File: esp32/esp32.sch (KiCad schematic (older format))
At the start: 54 parts, among them IC1 KF33BDT-TR, J1 USB_C_Receptacle_2.0, Q1 FDS9926A, Q2 FDN306P, Q3 BC817, Q4 BC817, SW1 ON-OFF, SW2 Reset, SW3 Boot, U1 AP5056, U2 DW01A, U3 CP2102, U4 ESP32-WROOM-32

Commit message: Add PCB routing
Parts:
- added J2, J3: Conn_01x16, Connector_PinHeader_2.54mm:PinHeader_1x16_P2.54mm_Vertical, symbol Connector_Generic:Conn_01x16
- BT1: footprint BatteryHolder:BatteryHolder_SMT_1x26650 -> TerminalBlock_MetzConnect:TerminalBlock_MetzConnect_Type055_RT01502HDWU_1x02_P5.00mm_Horizontal
- J1: value USB_C_Receptacle_2.0 -> USB_C
- SW3: footprint Button_Switch_SMD:SW_SPST_B3U-1000P-B -> Button_Switch_SMD:SW_SPST_B3U-1000P
- U1: symbol CP2102:AP5056 -> esp32-rescue:AP5056-CP2102
- U2: renamed from U3; symbol CP2102:CP2102 -> esp32-rescue:CP2102-CP2102
- renumbered C9 to C10, C10 to C11, C11 to C12, C3 to C13, C13 to C14, C4 to C3, C5 to C4, C12 to C5, C14 to C7, C7 to C8, C8 to C9, U4 to ESP32, Q2 to Q1, Q1 to Q2, R12 to R10, R13 to R11, R14 to R12, R15 to R13, R4 to R14, R16 to R15, R17 to R16, R18 to R17, R9 to R18, R5 to R4, R6 to R5, R7 to R6, R8 to R7, R10 to R8, R11 to R9, U2 to U3
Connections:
- net labels added: 10, 11, 12, 13, 14, 16, 23, 24, 26, 27, 28, 29, 30, 31, 33, 36, 37, 4, 5, 6, 7, 8, 9, Rx, Temp, Tx
- wire segments 228 -> 290
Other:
- note added: "3.3V Regulator"
- note added: "Auto-Reset"
- note added: "Battery Charger"
- note added: "Battery Protection"
- note added: "Pin connector"
- note added: "Reset & Boot"
- note added: "USB to UART Bridge"
- note added: "USB-C Connector"
- note added: "Wi-Fi+BT Module"
- moved on the sheet: BT1, C1, C10, C11, C12, C13, C14, C2, C3, C4, C5, C6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

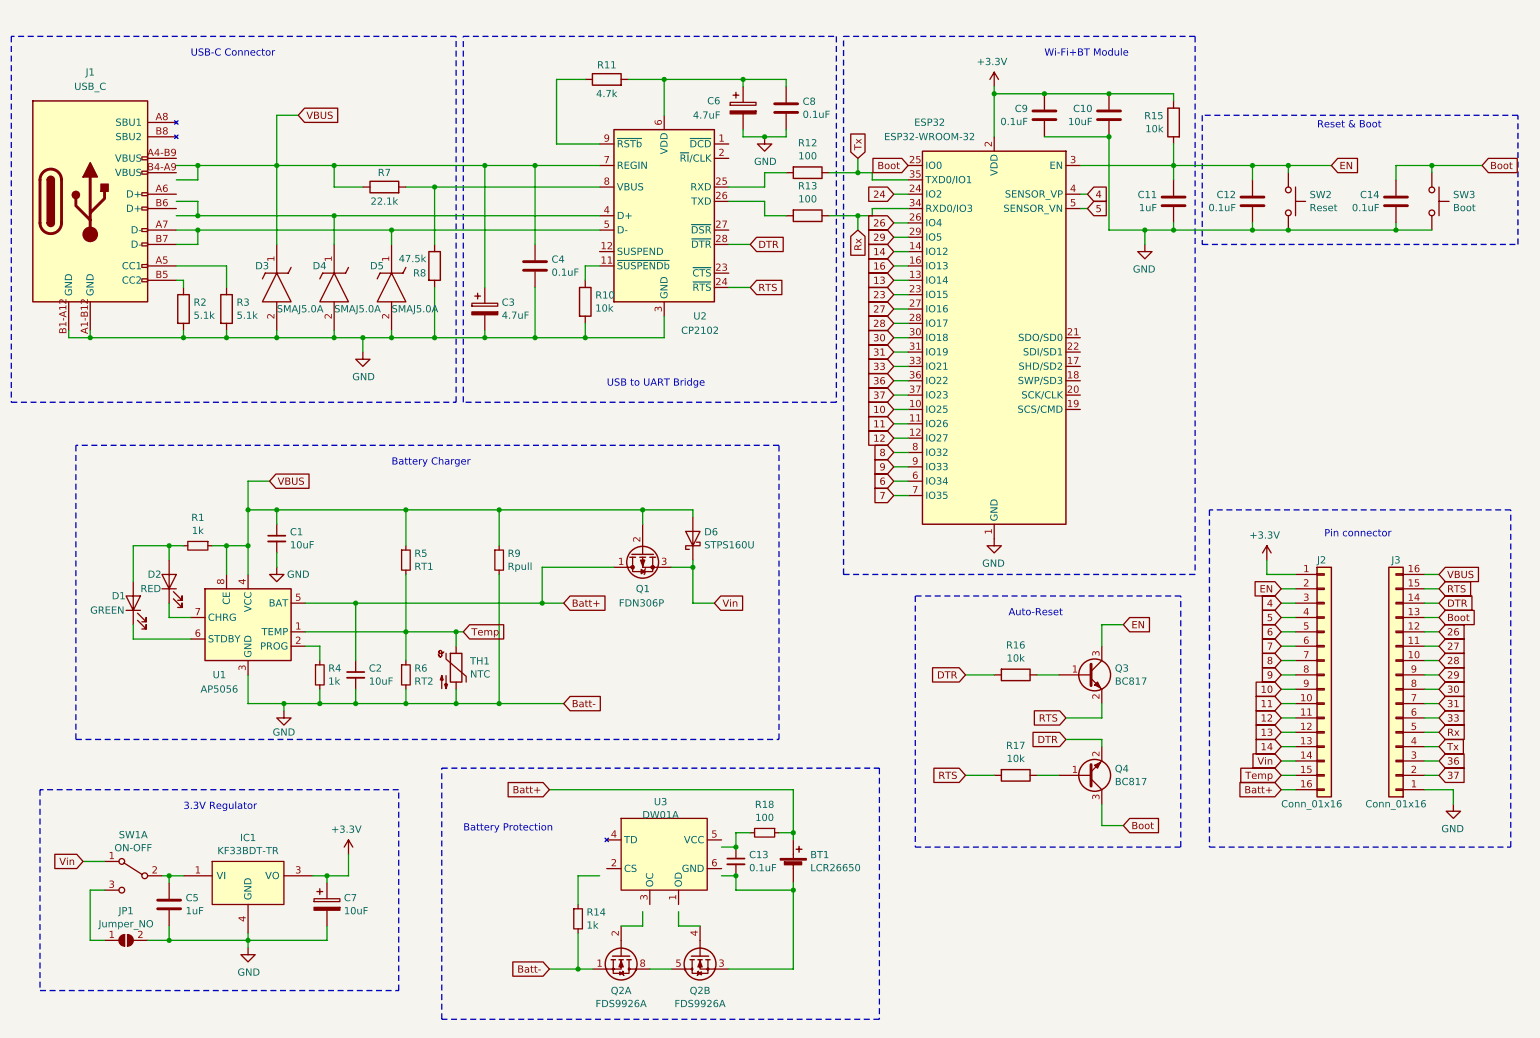
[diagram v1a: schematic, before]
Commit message: 1) Power tracks to 30 milis - 2) Add more pins for symmetry
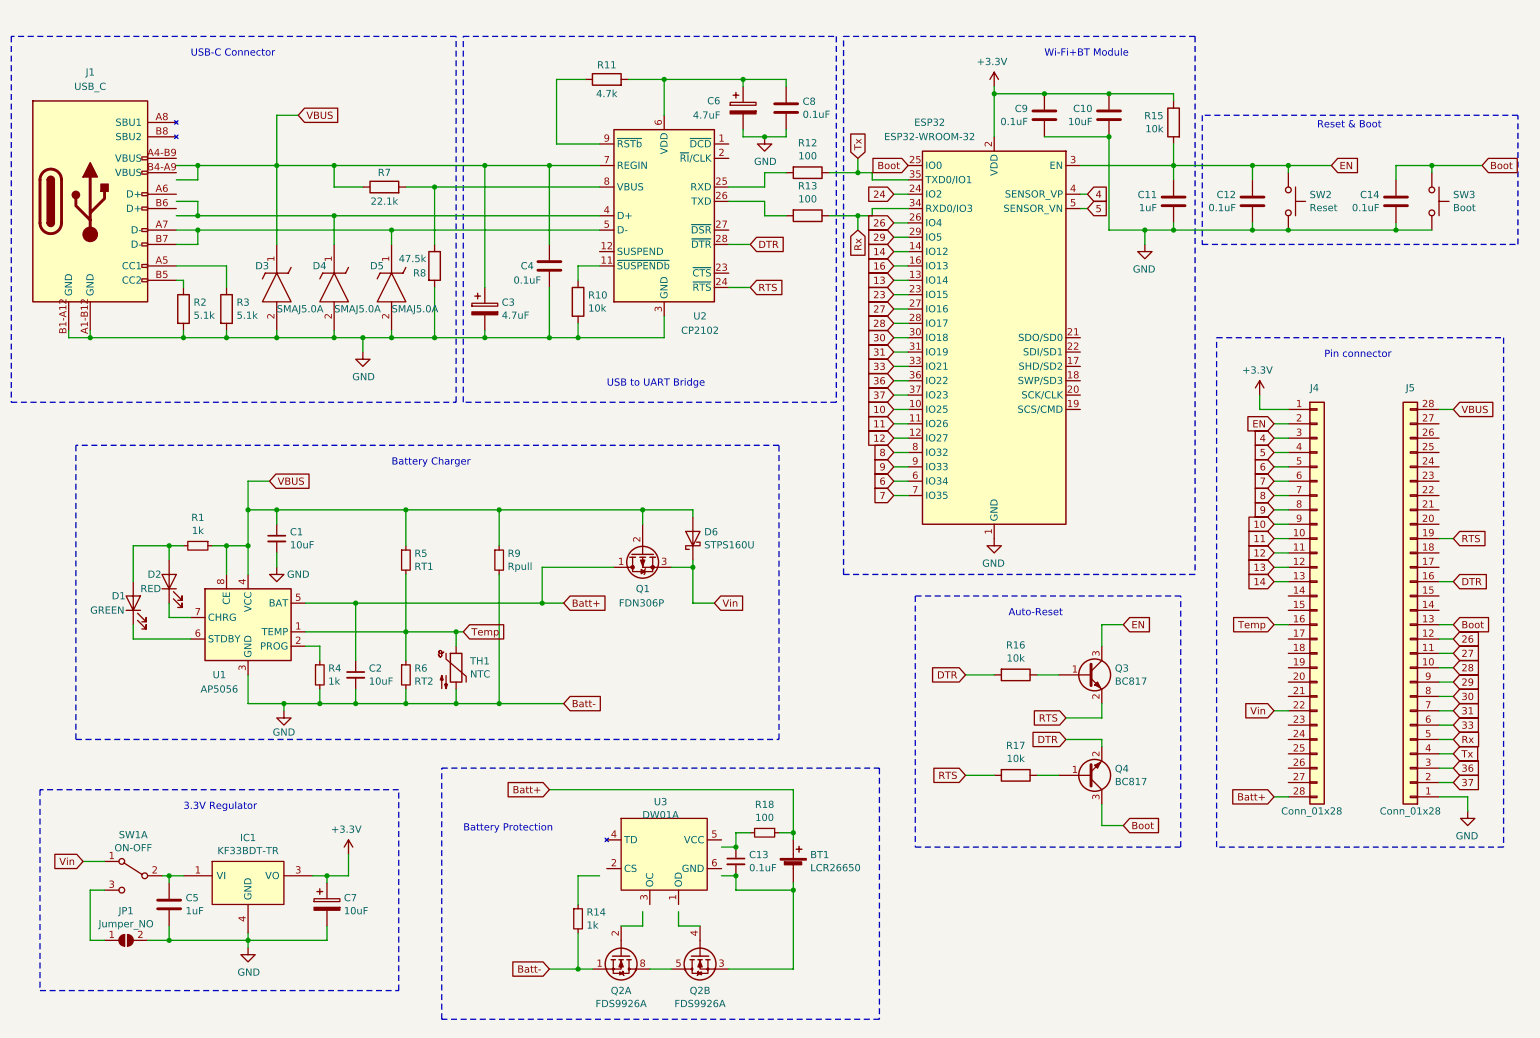
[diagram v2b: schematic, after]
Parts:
- removed J2, J3: Conn_01x16, Connector_PinHeader_2.54mm:PinHeader_1x16_P2.54mm_Vertical, symbol Connector_Generic:Conn_01x16
- added J4, J5: Conn_01x28, Connector_PinHeader_2.54mm:PinHeader_1x28_P2.54mm_Vertical, symbol Connector_Generic:Conn_01x28
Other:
- moved on the sheet: C4, R10

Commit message: Cambio de componentes: 1) USB-to-UART (CH340G por CP2102) 2) Dual Mosfet (8205A por FDS9926A)
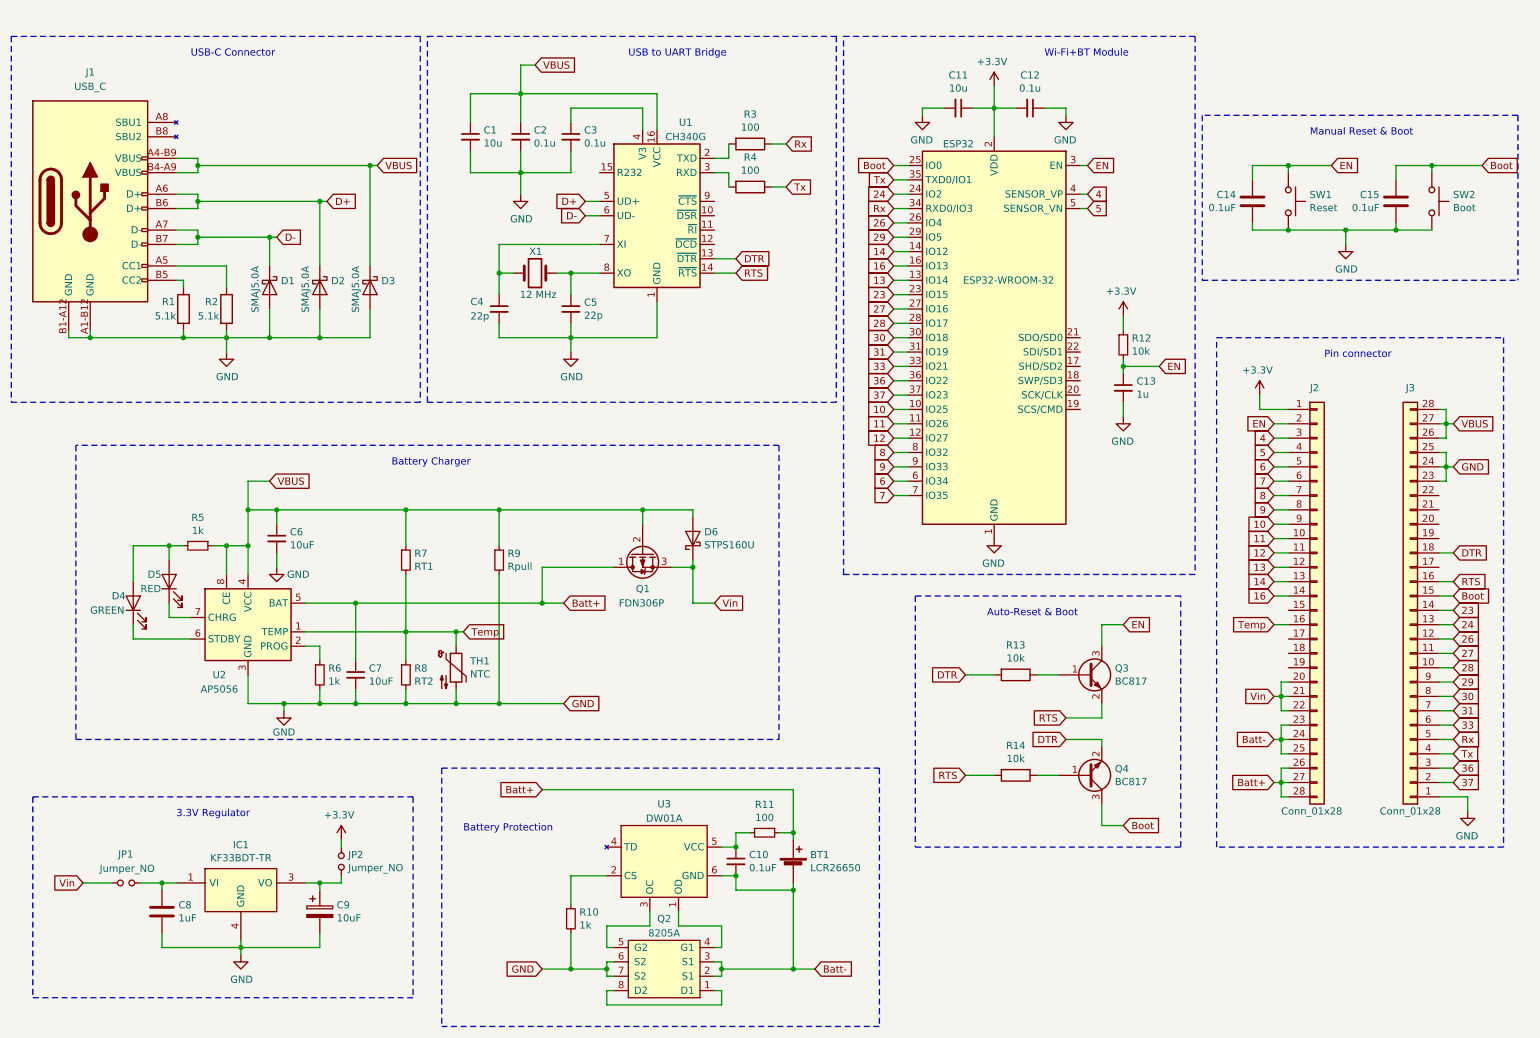
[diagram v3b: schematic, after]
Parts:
- removed C10: 10uF, Capacitor_SMD:C_0805_2012Metric_Pad1.15x1.40mm_HandSolder, symbol Device:C
- removed C11: 1uF, Capacitor_SMD:C_0805_2012Metric_Pad1.15x1.40mm_HandSolder, symbol Device:C
- removed C3, C6: 4.7uF, Capacitor_Tantalum_SMD:CP_EIA-3216-12_Kemet-S_Pad1.58x1.35mm_HandSolder, symbol Device:CP
- removed C4, C8, C9: 0.1uF, Capacitor_SMD:C_0805_2012Metric_Pad1.15x1.40mm_HandSolder, symbol Device:C
- removed D3, D4, D5: SMAJ5.0A, SMAJ5.0A:DIOM5026X229N, symbol SMAJ5.0A:SMAJ5.0A
- removed JP1: Jumper_NO, Jumper:SolderJumper-2_P1.3mm_Open_RoundedPad1.0x1.5mm, symbol Jumper:SolderJumper_2_Open
- removed Q2: FDS9926A, Package_SO:SOIC-8_3.9x4.9mm_P1.27mm, symbol Transistor_FET:FDS9926A
- removed R10, R15: 10k, Resistor_SMD:R_0805_2012Metric_Pad1.15x1.40mm_HandSolder, symbol Device:R
- removed R11: 4.7k, Resistor_SMD:R_0805_2012Metric_Pad1.15x1.40mm_HandSolder, symbol Device:R
- removed R7: 22.1k, Resistor_SMD:R_0805_2012Metric_Pad1.15x1.40mm_HandSolder, symbol Device:R
- removed R8: 47.5k, Resistor_SMD:R_0805_2012Metric_Pad1.15x1.40mm_HandSolder, symbol Device:R
- removed SW1: ON-OFF, Button_Switch_SMD:SW_SPDT_PCM12, symbol Switch:SW_DPDT_x2
- removed U2: CP2102, Package_DFN_QFN:QFN-28-1EP_5x5mm_P0.5mm_EP3.35x3.35mm, symbol esp32-rescue:CP2102-CP2102
- added C1, C11: 10u, Capacitor_SMD:C_0805_2012Metric_Pad1.15x1.40mm_HandSolder, symbol Device:C_Small
- added C12, C2, C3: 0.1u, Capacitor_SMD:C_0805_2012Metric_Pad1.15x1.40mm_HandSolder, symbol Device:C_Small
- added C13: 1u, Capacitor_SMD:C_0805_2012Metric_Pad1.15x1.40mm_HandSolder, symbol Device:C_Small
- added C4, C5: 22p, Capacitor_SMD:C_0805_2012Metric_Pad1.15x1.40mm_HandSolder, symbol Device:C_Small
- added D1, D2, D3: SMAJ5.0A, SMAJ5.0A:DIOM5026X229N, symbol Device:D_Schottky
- added JP1, JP2: Jumper_NO, Connector_PinSocket_2.54mm:PinSocket_1x02_P2.54mm_Vertical, symbol Device:Jumper_NO_Small
- added Q2: 8205A, Package_SO:TSSOP-8_4.4x3mm_P0.65mm, symbol 8205A:8205A
- added R12: 10k, Resistor_SMD:R_0805_2012Metric_Pad1.15x1.40mm_HandSolder, symbol Device:R_Small
- added U1: CH340G, Package_SO:SOIC-16_3.9x9.9mm_P1.27mm, symbol Interface_USB:CH340G
- added X1: 12 MHz, Crystal:Crystal_HC18-U_Vertical, symbol Device:Crystal
- C9: renamed from C7; footprint Capacitor_THT:CP_Radial_D6.3mm_P2.50mm -> Capacitor_THT:CP_Radial_D4.0mm_P2.00mm
- renumbered C13 to C10, C12 to C14, C14 to C15, C1 to C6, C2 to C7, C5 to C8, D1 to D4, D2 to D5, J4 to J2, J5 to J3, R2 to R1, R14 to R10, R18 to R11, R16 to R13, R17 to R14, R3 to R2, R12 to R3, R13 to R4, R1 to R5, R4 to R6, R5 to R7, R6 to R8, SW2 to SW1, SW3 to SW2, U1 to U2
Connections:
- net labels added: D+, D-
- wire segments 290 -> 322
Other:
- note added: "Auto-Reset & Boot"
- note added: "Manual Reset & Boot"
- note removed: "Auto-Reset"
- note removed: "Reset & Boot"
- moved on the sheet: C8, C9, IC1, R10, R3, R4, U3

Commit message: 1) Medicion de bateria - 2) Agujeros para tornillos - 3) Nombre de integarntes y proyecto
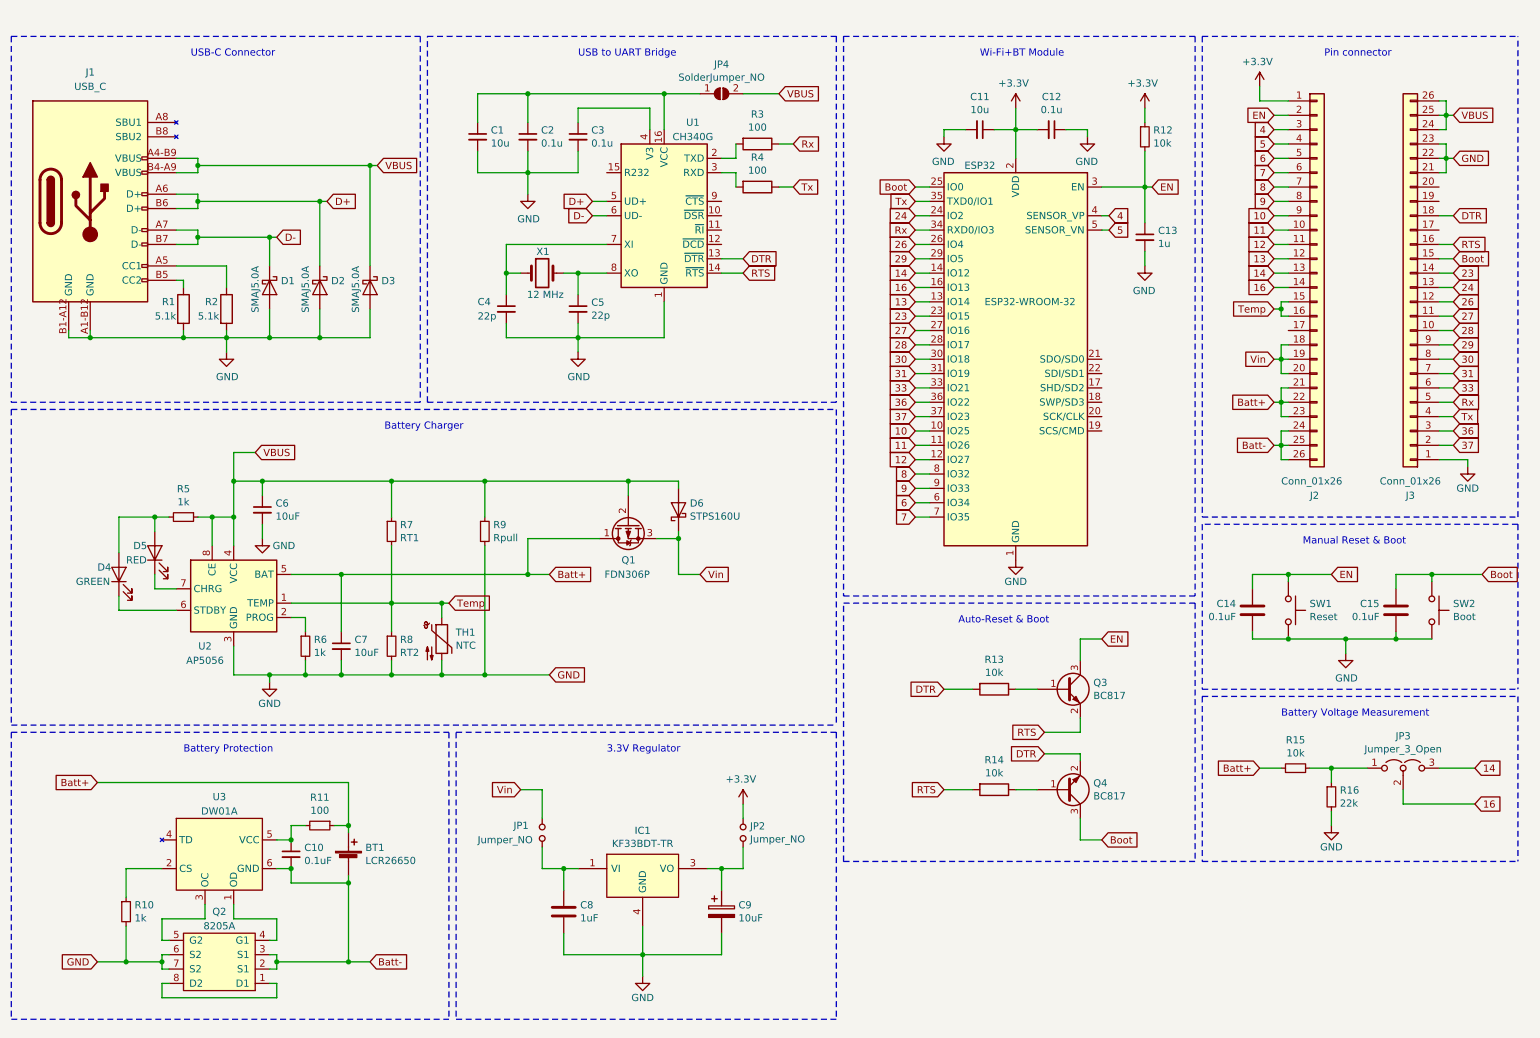
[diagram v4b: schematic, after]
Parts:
- removed J2, J3: Conn_01x28, Connector_PinHeader_2.54mm:PinHeader_1x28_P2.54mm_Vertical, symbol Connector_Generic:Conn_01x28
- added J2, J3: Conn_01x26, Connector_PinHeader_2.54mm:PinHeader_1x26_P2.54mm_Vertical, symbol Connector_Generic:Conn_01x26
- added JP3: Jumper_3_Open, Connector_PinSocket_2.54mm:PinSocket_1x03_P2.54mm_Vertical, symbol Jumper:Jumper_3_Open
- added JP4: SolderJumper_NO, Jumper:SolderJumper-2_P1.3mm_Open_RoundedPad1.0x1.5mm, symbol Jumper:SolderJumper_2_Open
- added R15: 10k, Resistor_SMD:R_0805_2012Metric_Pad1.15x1.40mm_HandSolder, symbol Device:R_Small
- added R16: 22k, Resistor_SMD:R_0805_2012Metric_Pad1.15x1.40mm_HandSolder, symbol Device:R_Small
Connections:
- net +3V3: now also J2.1 (Pin_1)
- net 10: now also J2.9 (Pin_9)
- net 11: now also J2.10 (Pin_10)
- net 12: now also J2.11 (Pin_11)
- net 13: now also J2.12 (Pin_12)
- net 14: now also J2.13 (Pin_13), JP3.3 (B)
- net 16: now also J2.14 (Pin_14), JP3.2 (C)
- net 23: now also J3.14 (Pin_14)
- net 24: now also J3.13 (Pin_13)
- net 26: now also J3.12 (Pin_12)
- net 27: now also J3.11 (Pin_11)
- net 28: now also J3.10 (Pin_10)
- net 29: now also J3.9 (Pin_9)
- net 30: now also J3.8 (Pin_8)
- net 31: now also J3.7 (Pin_7)
- net 33: now also J3.6 (Pin_6)
- net 36: now also J3.3 (Pin_3)
- net 37: now also J3.2 (Pin_2)
- net 4: now also J2.3 (Pin_3)
- net 5: now also J2.4 (Pin_4)
- net 6: now also J2.5 (Pin_5)
- net 7: now also J2.6 (Pin_6)
- net 8: now also J2.7 (Pin_7)
- net 9: now also J2.8 (Pin_8)
- net Batt+: now also J2.21 (Pin_21), J2.22 (Pin_22), J2.23 (Pin_23), R15.1
- net Batt-: now also J2.24 (Pin_24), J2.25 (Pin_25), J2.26 (Pin_26)
- net Boot: now also J3.15 (Pin_15)
- net DTR: now also J3.18 (Pin_18)
- net EN: now also J2.2 (Pin_2)
- net GND: now also J3.1 (Pin_1), J3.21 (Pin_21), J3.22 (Pin_22), J3.23 (Pin_23), R16.2
- net RTS: now also J3.16 (Pin_16)
- net Rx: now also J3.5 (Pin_5)
- net Temp: now also J2.15 (Pin_15), J2.16 (Pin_16)
- net Tx: now also J3.4 (Pin_4)
- net VBUS: now also J3.24 (Pin_24), J3.25 (Pin_25), J3.26 (Pin_26), JP4.2 (B); no longer C1.1, C2.1, U1.16 (VCC)
- net Vin: now also JP1.2, J2.18 (Pin_18), J2.19 (Pin_19), J2.20 (Pin_20); no longer JP1.1
- net at C8.1, IC1.1 (VI): now also JP1.1; no longer JP1.2
- new net: JP3.1 (A), R15.2, R16.1
- new net: C1.1, C2.1, JP4.1 (A), U1.16 (VCC)
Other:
- note added: "Battery Voltage Measurement"
- moved on the sheet: BT1, C1, C10, C11, C12, C13, C14, C15, C2, C3, C4, C5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
